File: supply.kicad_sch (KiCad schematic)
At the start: 106 parts, among them J12 Molex_Nano-Fit-105430_xx02-ho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, Q11 PJE138K, Q13 BCM857BS-7-F, Q14 BCM857BS-7-F, Q15 SSM3J332R, Q16 SSM3J332R, Q18 SSM3J332R, Q5 PJE138K, Q6 SSM3J332R, Q7 PJE138K, Q8 PJE138K, SW1 PCM12SMTR, U1 TPS56C230, U29 TPS56C230, U37 74LVC2G14GV, U38 74LVC1G175GV, U41 NCP730BMT330TBG, U42 TPS7A0518PDBVT

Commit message: Renaming Sheets
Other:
- company: Antmicro Ltd -> Dronolab
- title: Jetson Orin Baseboard -> Supply
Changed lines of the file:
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@@
   (paper "A3")
   (title_block
-    (title "Jetson Orin Baseboard")
-    (date "2023-03-03")
-    (rev "1.1.0")
-    (company "Antmicro Ltd")
-    (comment 1 "www.antmicro.com")
+    (title "Supply")
+    (date "2023-07-05")
+    (rev "1.0.0")
+    (company "Dronolab")
+    (comment 1 "dronolab.etsmtl.ca")
   )
   (junction (at 69.215 52.07) (diameter 0) (color 0 0 0 0)

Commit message: Simplification continues
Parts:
- removed Q14: BCM857BS-7-F, jetson-orin-baseboard-footprints:SOT-363, symbol jetson-orin-baseboard:BCM857BS-7-F
- removed Q16: SSM3J332R, jetson-orin-baseboard-footprints:SOT-23-3, symbol jetson-orin-baseboard:SSM3J332R
- removed R251, R255: R_10k_0402, jetson-orin-baseboard-footprints:0402-res, symbol jetson-orin-baseboard:R_10k_0402
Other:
- moved on the sheet: R252, R253

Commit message: Schematic Done
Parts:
- removed R253: R_0R_0603_HPWR, jetson-orin-baseboard-footprints:0603-res, symbol jetson-orin-baseboard:R_0R_0603_HPWR
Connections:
- net USBPD1_HV renamed USBPD_HV
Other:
- moved on the sheet: C103, C116, C117, C120, C121, C122, C123, C125, C126, C127, C128, C129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

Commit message: Schematic V1 and footprints assigned
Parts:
- renumbered C124 to C100, C6 to C101, C122 to C102, C93 to C103, C123 to C104, C102 to C105, C125 to C106, C83 to C107, C134 to C108, C103 to C109, C126 to C110, C129 to C111, C127 to C112, C120 to C113, C128 to C114, C153 to C115, C154 to C116, C137 to C117, C142 to C118, C116 to C90, C117 to C91, C150 to C92, C118 to C93, C50 to C94, C119 to C95, C5 to C96, C151 to C97, C152 to C98, C121 to C99, D60 to D45, D28 to D46, D36 to D47, D37 to D48, D53 to D49, D29 to D50, D61 to D51, D32 to D52, D33 to D53, D30 to D54, D31 to D55, Q11 to Q10, Q8 to Q11, Q5 to Q12, Q6 to Q13, Q13 to Q6, Q15 to Q8, Q18 to Q9, R249 to R120, R250 to R121, R252 to R122, R254 to R123, R256 to R124, R257 to R125, R236 to R126, R164 to R127, R258 to R128, R165 to R129, R175 to R130, R188 to R131, R259 to R132, R260 to R133, R261 to R134, R183 to R135, R263 to R136, R237 to R137, R159 to R138, R238 to R139, R173 to R140, R264 to R141, R239 to R142, R240 to R143, R169 to R144, R170 to R145, R176 to R146, R177 to R147, R268 to R148, R172 to R149, R178 to R150, R273 to R151, R181 to R152, R276 to R153, R182 to R154, TP14 to TP21, TP23 to TP22, TP54 to TP23, TP52 to TP24, TP55 to TP25, TP53 to TP26, U37 to U22, U38 to U23, U1 to U24, U29 to U25, U41 to U26, U42 to U27
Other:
- moved on the sheet: C106, D53, R147, TP23

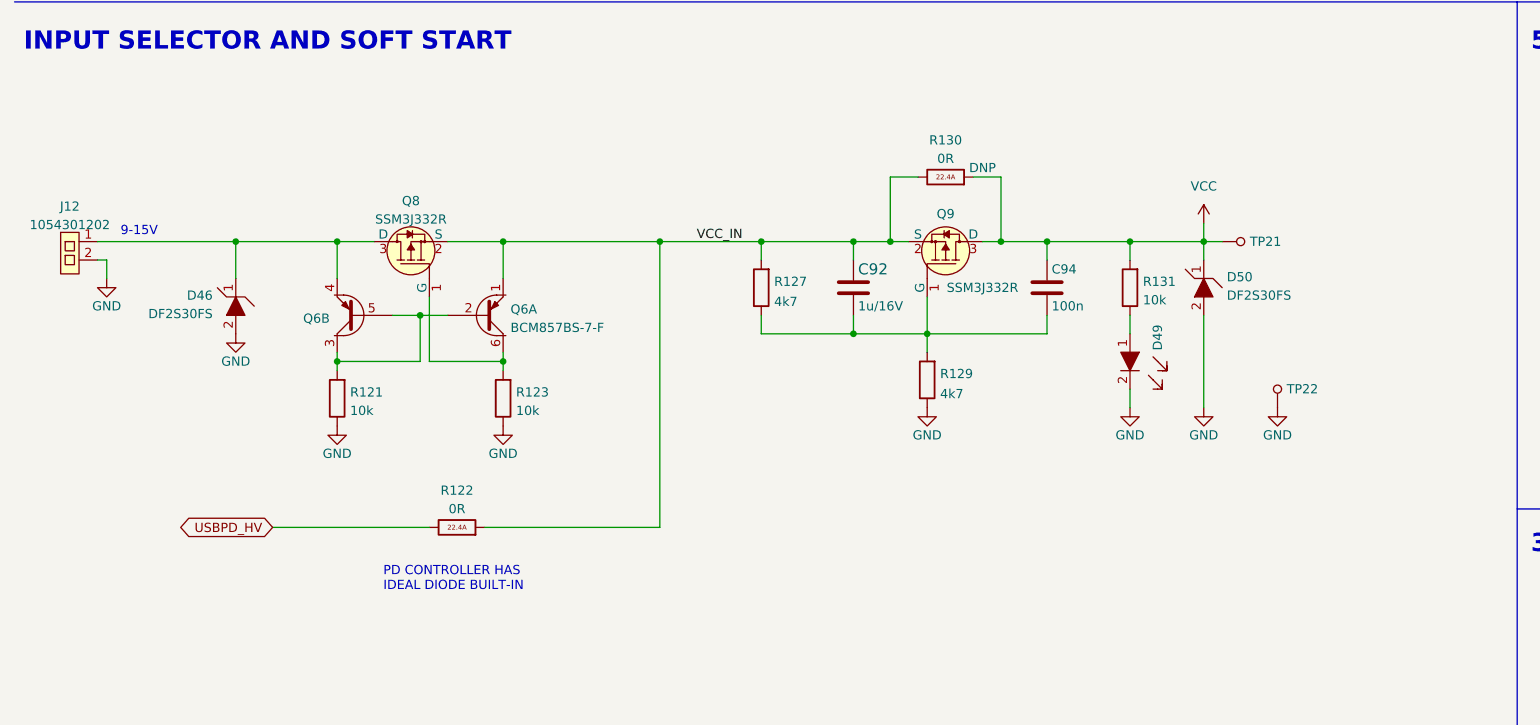
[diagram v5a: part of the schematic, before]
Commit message: Footprints well assigned, XT30 added, Shields grounded
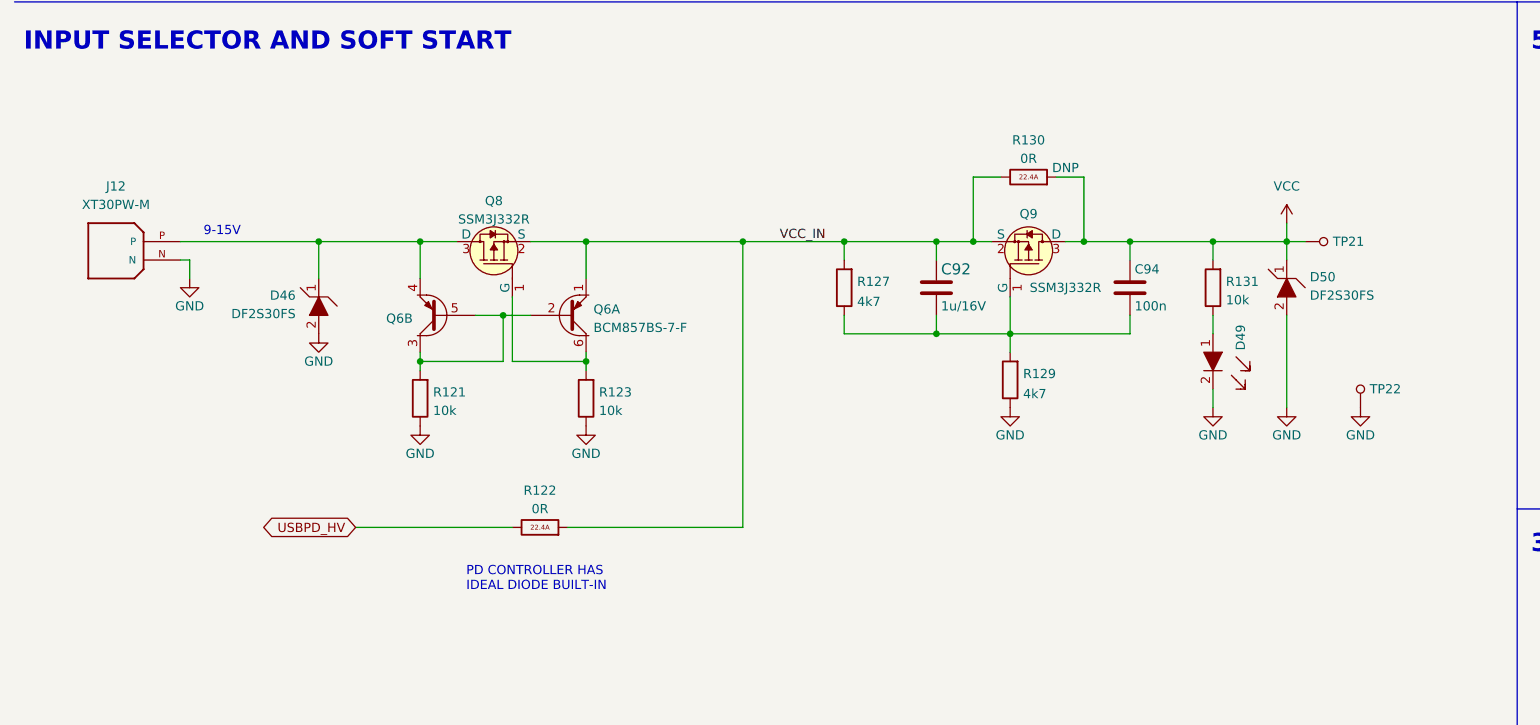
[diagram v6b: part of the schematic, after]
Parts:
- removed J12: Molex_Nano-Fit-105430_xx02-horizontal, jetson-orin-baseboard-footprints:Molex_Nano-Fit_105430-xx02_1x02_P2.50mm_Horizontal_SMD, symbol jetson-orin-baseboard:Molex_Nano-Fit-105430_xx02-horizontal
- added J12: XT30PW-M, jetson-orin-baseboard-footprints:AMASS_XT30PW-M, symbol XT30PW-M:XT30PW-M
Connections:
- net GND: now also J12.N, J12.S1, J12.S2
- net at D46.1, Q6.4, Q8.3 (D): now also J12.P
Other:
- moved on the sheet: C92, C94, D46, D49, D50, Q6A, Q6B, Q8, Q9, R121, R122, R123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
